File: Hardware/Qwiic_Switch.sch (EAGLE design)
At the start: 23 parts, among them J7 ISP, U4 ATTINY84-ARDUINO

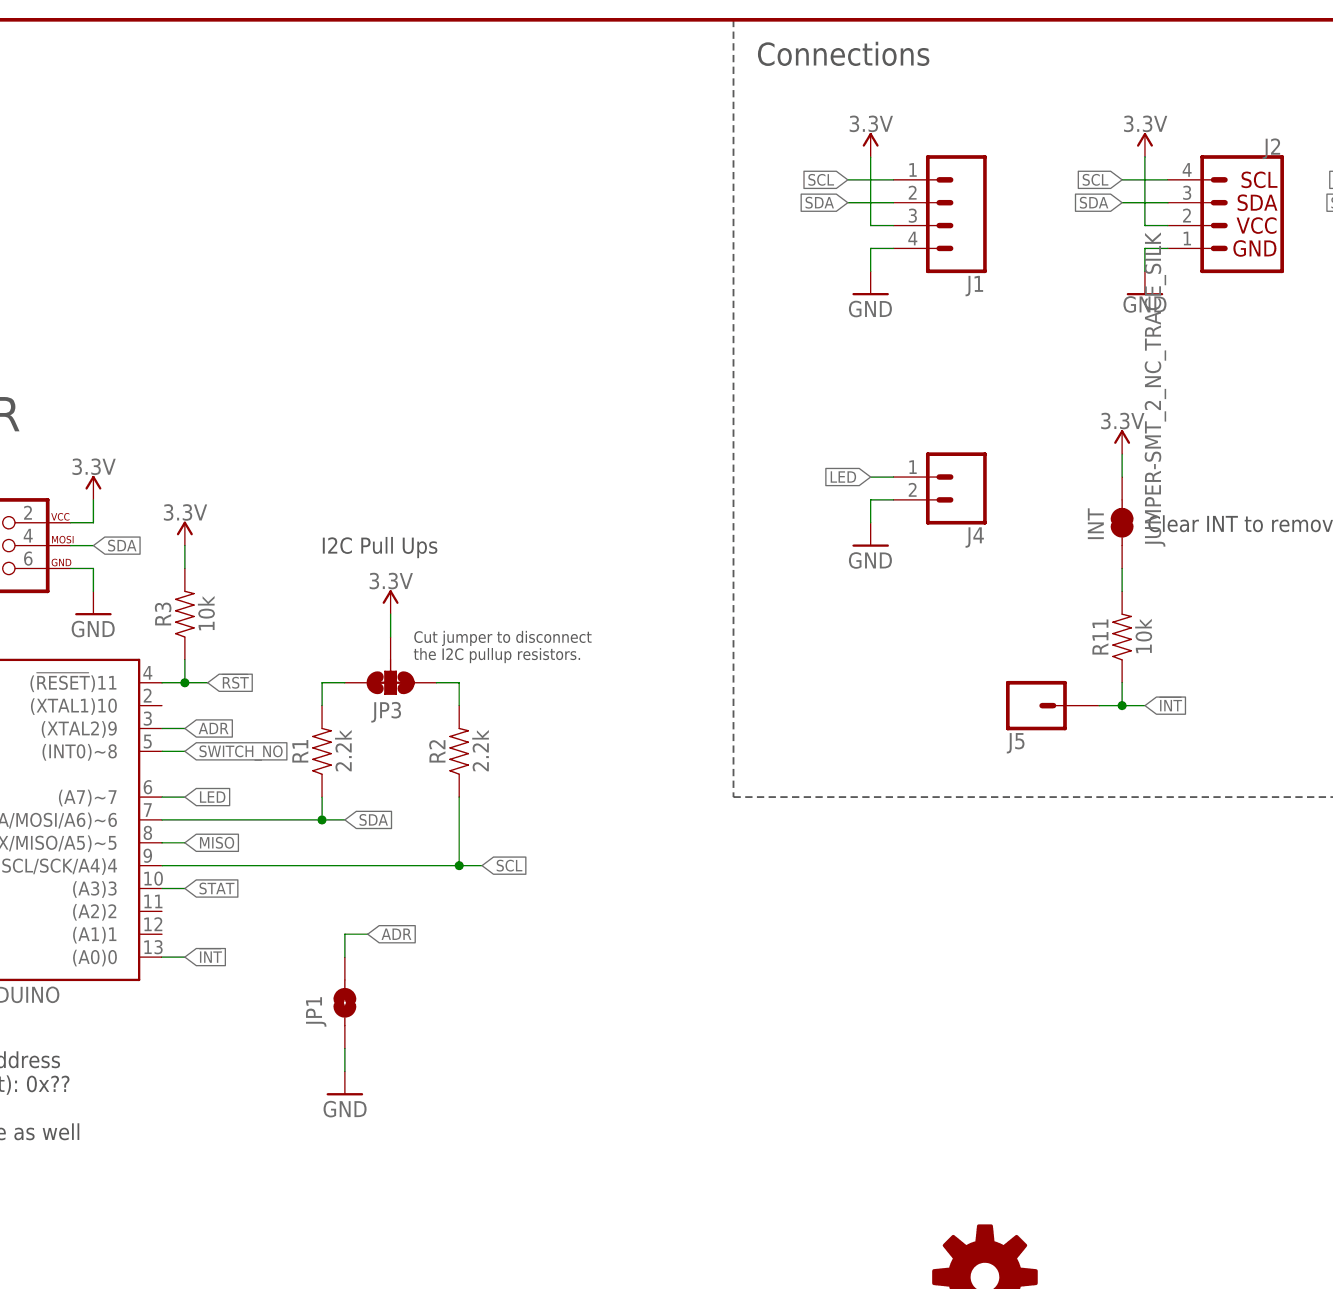
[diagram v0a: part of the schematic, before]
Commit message: Add ADR jumpers. Decrease leaf switch gap to 0.025". Remove old files.
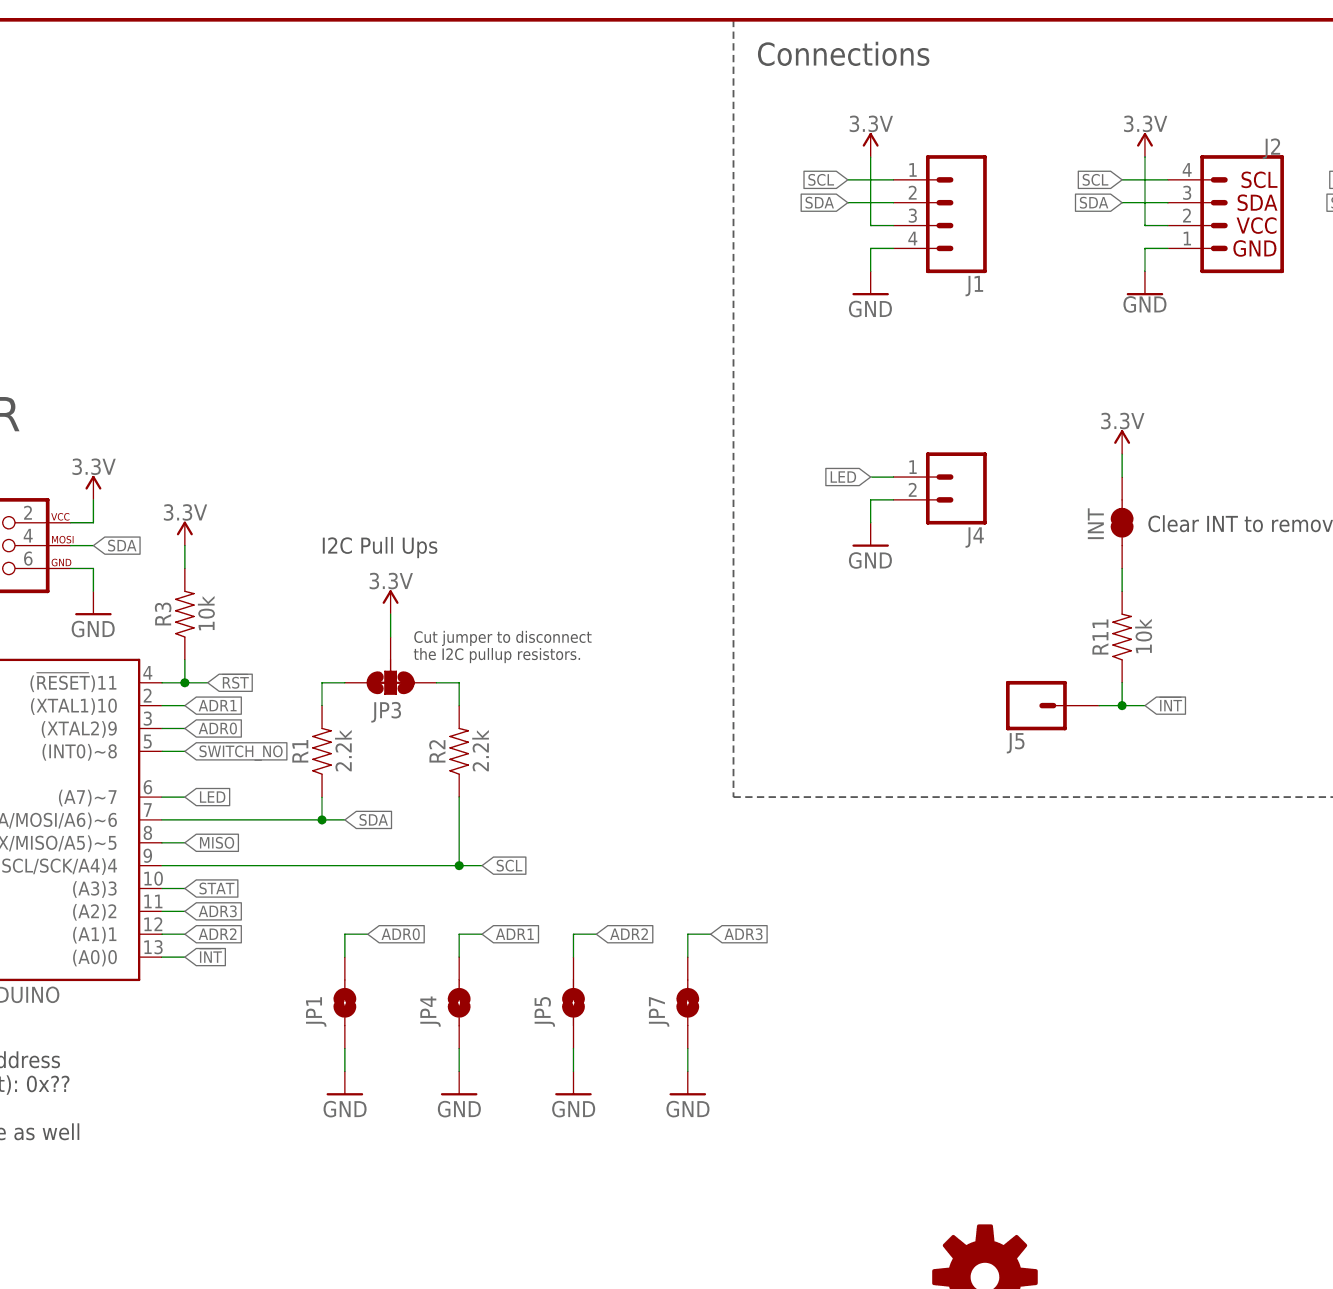
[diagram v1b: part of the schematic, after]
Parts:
- added JP4, JP5, JP7: JUMPER-SMT_2_NO_SILK, SparkFun-Jumpers:JUMPER-SMT_2_NO_SILK
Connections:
- net ADR renamed ADR0
- new net ADR1: JP4.2, U4.(XTAL1)10
- new net ADR2: JP5.2, U4.(A1)1
- new net ADR3: JP7.2, U4.(A2)2
- net GND: now also JP4.1, JP5.1, JP7.1
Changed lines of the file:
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@@
 <?xml version="1.0" encoding="utf-8"?>
 <!DOCTYPE eagle SYSTEM "eagle.dtd">
-<eagle version="9.4.0">
+<eagle version="9.4.2">
 <drawing>
 <settings>
@@
 <part name="R11" library="SparkFun-Resistors" deviceset="10KOHM" device="-0603-1/10W-1%" value="10k"/>
 <part name="SUPPLY5" library="SparkFun-PowerSymbols" deviceset="3.3V" device=""/>
-<part name="INT" library="SparkFun-Jumpers" deviceset="JUMPER-SMT_2_NC_TRACE" device="_SILK" value="JUMPER-SMT_2_NC_TRACE_SILK"/>
+<part name="INT" library="SparkFun-Jumpers" deviceset="JUMPER-SMT_2_NC_TRACE" device="_SILK" value=""/>
 <part name="J4" library="SparkFun-Connectors" deviceset="CONN_02" device="1X02_NO_SILK"/>
 <part name="GND1" library="SparkFun" deviceset="GND" device=""/>
+<part name="GND2" library="SparkFun" deviceset="GND" device=""/>
+<part name="JP4" library="SparkFun-Jumpers" deviceset="JUMPER-SMT_2_NO" device="_SILK" value=""/>
+<part name="GND3" library="SparkFun" deviceset="GND" device=""/>
+<part name="JP5" library="SparkFun-Jumpers" deviceset="JUMPER-SMT_2_NO" device="_SILK" value=""/>
+<part name="GND5" library="SparkFun" deviceset="GND" device=""/>
+<part name="JP7" library="SparkFun-Jumpers" deviceset="JUMPER-SMT_2_NO" device="_SILK" value=""/>
 </parts>
 <sheets>
@@
 <attribute name="VALUE" x="160.02" y="124.46" size="1.778" layer="96"/>
 </instance>
+<instance part="GND2" gate="1" x="116.84" y="66.04" smashed="yes" rot="MR0">
+<attribute name="VALUE" x="119.38" y="63.5" size="1.778" layer="96" rot="MR0"/>
+</instance>
+<instance part="JP4" gate="G$1" x="116.84" y="76.2" smashed="yes" rot="R90">
+<attribute name="NAME" x="114.3" y="73.66" size="1.778" layer="95" font="vector" rot="R90"/>
+<attribute name="VALUE" x="119.38" y="73.66" size="1.778" layer="96" font="vector" rot="R90" align="top-left"/>
+</instance>
+<instance part="GND3" gate="1" x="129.54" y="66.04" smashed="yes" rot="MR0">
+<attribute name="VALUE" x="132.08" y="63.5" size="1.778" layer="96" rot="MR0"/>
+</instance>
+<instance part="JP5" gate="G$1" x="129.54" y="76.2" smashed="yes" rot="R90">
+<attribute name="NAME" x="127" y="73.66" size="1.778" layer="95" font="vector" rot="R90"/>
+<attribute name="VALUE" x="132.08" y="73.66" size="1.778" layer="96" font="vector" rot="R90" align="top-left"/>
+</instance>
+<instance part="GND5" gate="1" x="142.24" y="66.04" smashed="yes" rot="MR0">
+<attribute name="VALUE" x="144.78" y="63.5" size="1.778" layer="96" rot="MR0"/>
+</instance>
+<instance part="JP7" gate="G$1" x="142.24" y="76.2" smashed="yes" rot="R90">
+<attribute name="NAME" x="139.7" y="73.66" size="1.778" layer="95" font="vector" rot="R90"/>
+<attribute name="VALUE" x="144.78" y="73.66" size="1.778" layer="96" font="vector" rot="R90" align="top-left"/>
+</instance>
 </instances>
 <busses>
@@
 <wire x1="162.56" y1="132.08" x2="162.56" y2="129.54" width="0.1524" layer="91"/>
 <pinref part="GND1" gate="1" pin="GND"/>
+</segment>
+<segment>
+<wire x1="116.84" y1="71.12" x2="116.84" y2="68.58" width="0.1524" layer="91"/>
+<pinref part="GND2" gate="1" pin="GND"/>
+<pinref part="JP4" gate="G$1" pin="1"/>
+</segment>
+<segment>
+<wire x1="129.54" y1="71.12" x2="129.54" y2="68.58" width="0.1524" layer="91"/>
+<pinref part="GND3" gate="1" pin="GND"/>
+<pinref part="JP5" gate="G$1" pin="1"/>
+</segment>
+<segment>
+<wire x1="142.24" y1="71.12" x2="142.24" y2="68.58" width="0.1524" layer="91"/>
+<pinref part="GND5" gate="1" pin="GND"/>
+<pinref part="JP7" gate="G$1" pin="1"/>
 </segment>
 </net>
@@
 </segment>
 </net>
-<net name="ADR" class="0">
+<net name="ADR0" class="0">
 <segment>
 <label x="106.68" y="83.82" size="1.27" layer="95" xref="yes"/>
@@
 </segment>
 </net>
+<net name="ADR1" class="0">
+<segment>
+<pinref part="U4" gate="U1" pin="(XTAL1)10"/>
+<wire x1="83.82" y1="109.22" x2="86.36" y2="109.22" width="0.1524" layer="91"/>
+<label x="86.36" y="109.22" size="1.27" layer="95" xref="yes"/>
+</segment>
+<segment>
+<label x="119.38" y="83.82" size="1.27" layer="95" xref="yes"/>
+<wire x1="116.84" y1="83.82" x2="119.38" y2="83.82" width="0.1524" layer="91"/>
+<wire x1="116.84" y1="81.28" x2="116.84" y2="83.82" width="0.1524" layer="91"/>
+<pinref part="JP4" gate="G$1" pin="2"/>
+</segment>
+</net>
+<net name="ADR3" class="0">
+<segment>
+<pinref part="U4" gate="U1" pin="(A2)2"/>
+<wire x1="83.82" y1="86.36" x2="86.36" y2="86.36" width="0.1524" layer="91"/>
+<label x="86.36" y="86.36" size="1.27" layer="95" xref="yes"/>
+</segment>
+<segment>
+<label x="144.78" y="83.82" size="1.27" layer="95" xref="yes"/>
+<wire x1="142.24" y1="83.82" x2="144.78" y2="83.82" width="0.1524" layer="91"/>
+<wire x1="142.24" y1="81.28" x2="142.24" y2="83.82" width="0.1524" layer="91"/>
+<pinref part="JP7" gate="G$1" pin="2"/>
+</segment>
+</net>
+<net name="ADR2" class="0">
+<segment>
+<pinref part="U4" gate="U1" pin="(A1)1"/>
+<wire x1="83.82" y1="83.82" x2="86.36" y2="83.82" width="0.1524" layer="91"/>
+<label x="86.36" y="83.82" size="1.27" layer="95" xref="yes"/>
+</segment>
+<segment>
+<label x="132.08" y="83.82" size="1.27" layer="95" xref="yes"/>
+<wire x1="129.54" y1="83.82" x2="132.08" y2="83.82" width="0.1524" layer="91"/>
+<wire x1="129.54" y1="81.28" x2="129.54" y2="83.82" width="0.1524" layer="91"/>
+<pinref part="JP5" gate="G$1" pin="2"/>
+</segment>
+</net>
